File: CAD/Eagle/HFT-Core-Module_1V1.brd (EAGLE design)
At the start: 96.5 x 96.5 mm, 528 parts, among them Q0321 ABS07-32.768KHZ, Q1321 ABS07-32.768KHZ, Q2211 ABM3B-32.0000MHZ, Q2311 ABM3B-16.0000MHZ, T1051 MMBT2222, T1111 MMBT2222, T1121 MMBT2222, T1131 MMBT2222, U0111 STM32L4Z_144PIN_SMPS, U0521 PCAL6416APW, U0621 PCAL6416APW, U0711 IS25LP032D, U0721 IS25LP032D, U0801 CAT24C64, U0911 ZIO_EINK_1IN54, U1001 MIDAS_MCCOG21605B6W-FPTLWI, U1301 BNO085, U1401 BME680, U1501 LM4120IM5-3.0, U1511 MAX5217, U1531 CFPT-141-20MHZ, U1541 OPA354, U1542 LPV811, U1601 Si5338, U1651 TS5A23166, U1701 PCM1863, U1801 WM8523, U1901 SIM868, U2201 SX1262, U2271 PE4259, U2301 AX5243, U2401 LM53603-Q1, U2501 BQ24193, U2541 LPV811, U2601 BQ25570, U2681 TS5A23166, U2701 TPS62056, U2801 TPS62051, U2851 MCP4661-104E-MS, U2901 TS5A23166, U3001 TS5A23166, U3101 TS5A23166, U3201 TS5A23166, U3491 TS5A23166, U3492 TDK B4310, X1201 TTE_EN11-HSM, X1951 MICROSIM-8P_SDCARD-8P_MOLEX-1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, X2411 WIRE-TO-BOARD_5MM08_1X02, X2551 JST_S3B-XH-A, X2601 WIRE-TO-BOARD_5MM08_1X02, X3301 MOLEX 105017-0001, X3401 SMA_SMT_AMPHENOL-901-143, X3411 SAMTEC SMA-J-P-H-RA-TH1, X3471 SMA_SMT_AMPHENOL-901-143, SAM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, X3481 SMA_SMT_AMPHENOL-901-143, SAM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, X3491 SMA_SMT_AMPHENOL-901-143, SAM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, X3501 CUI SJ1-3535NS, X3511 CUI SJ1-3535NS, X3611 2X20/90_1MM27_HARWIN_M50-3202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, X3612 2X20/90_1MM27_HARWIN_M50-3202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, X3631 2X20/90_1MM27_HARWIN_M50-3202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, X3632 2X20/90_1MM27_HARWIN_M50-3202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

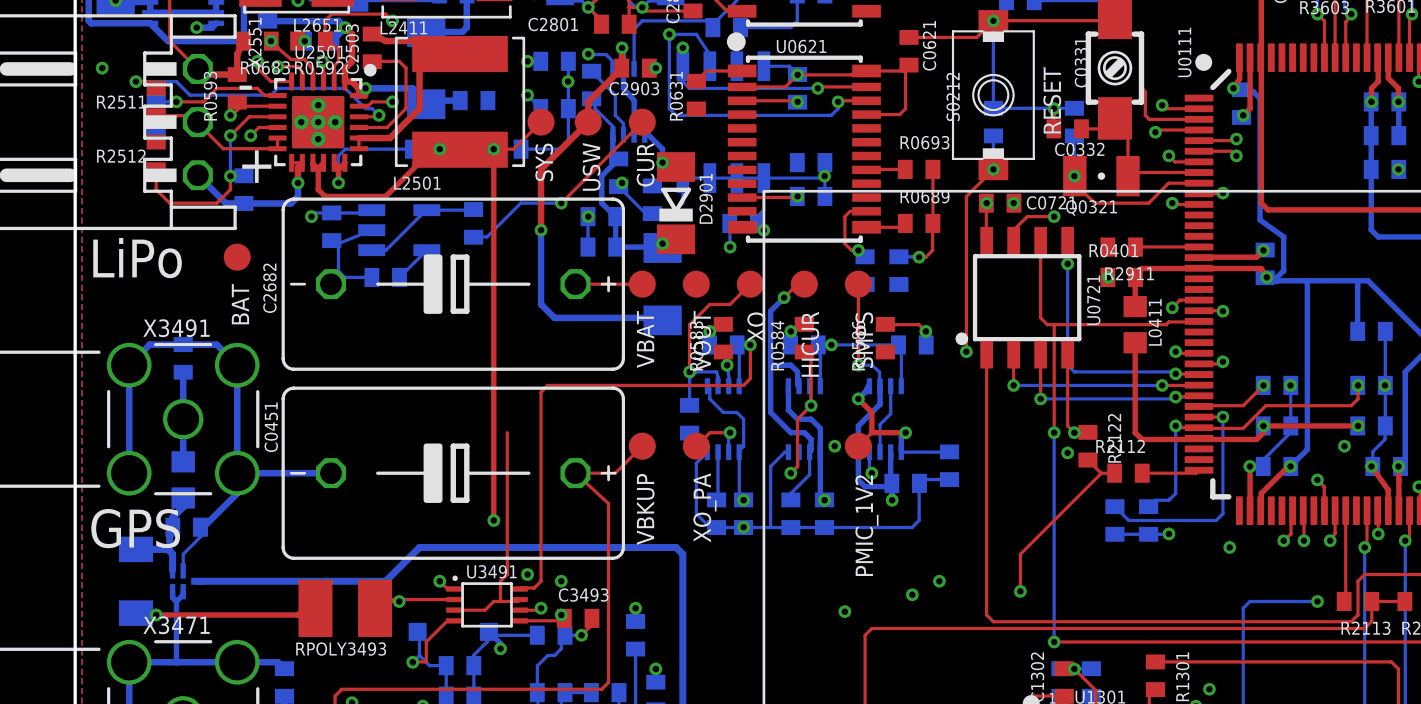
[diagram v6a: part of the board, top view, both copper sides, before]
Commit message: HW_1V1 - CAD/Eagle - MCU south complete
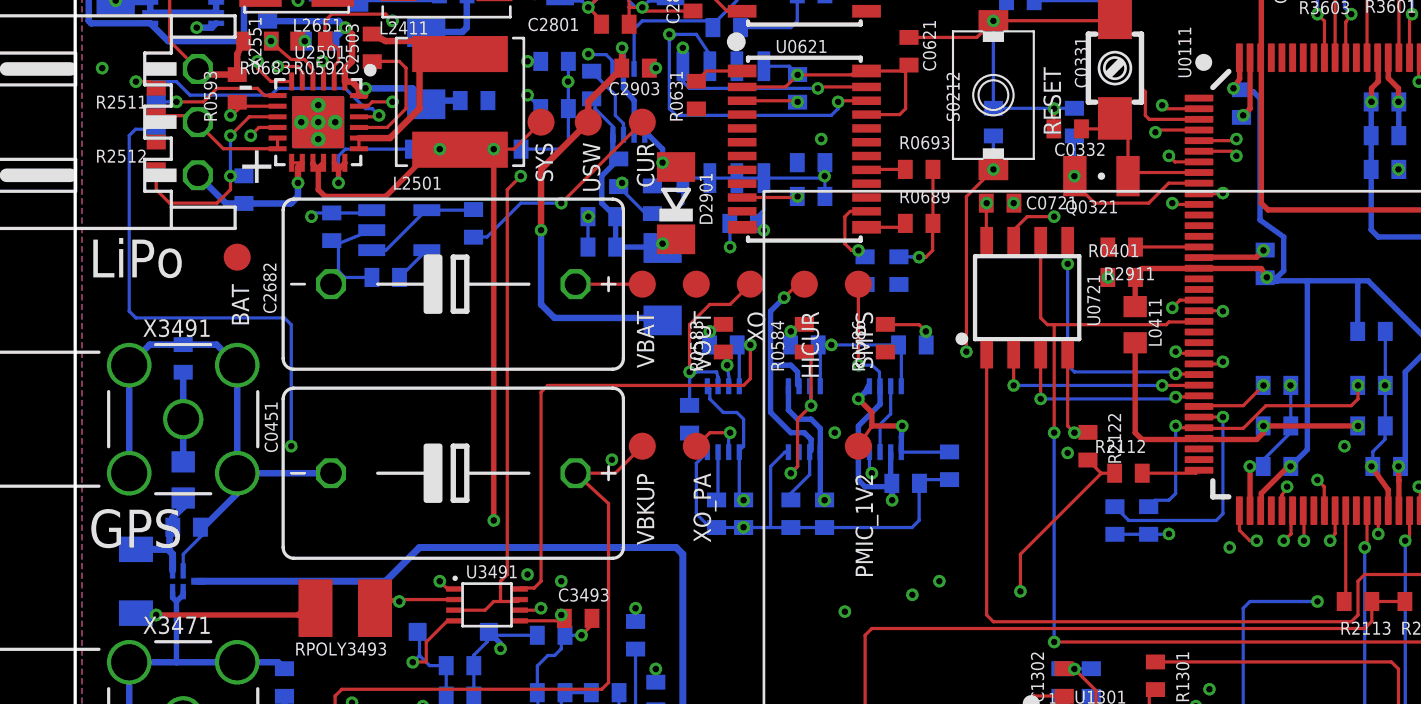
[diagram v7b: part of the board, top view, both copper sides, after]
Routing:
- net PA5: track 0.00 -> 72.1 mm, vias 0 -> 2
- net PA3: track 10.2 -> 57.6 mm, vias 1 -> 3
- net PEXPA_P1_2_R: track 13.7 -> 48.1 mm, vias 1 -> 3
- net PE3: track 76.8 -> 77.7 mm
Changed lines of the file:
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@@
 <wire x1="47.625" y1="53.0225" x2="46.6725" y2="53.0225" width="0.1524" layer="15"/>
 <via x="46.6725" y="53.0225" extent="1-16" drill="0.3"/>
-<wire x1="46.6725" y1="53.0225" x2="38.4175" y2="53.0225" width="0.1524" layer="3"/>
-<wire x1="38.4175" y1="53.0225" x2="38.1" y2="53.34" width="0.1524" layer="3"/>
-<wire x1="38.1" y1="53.34" x2="35.71875" y2="53.34" width="0.1524" layer="3"/>
-<via x="35.71875" y="53.34" extent="1-16" drill="0.3"/>
-<wire x1="35.71875" y1="53.34" x2="35.8775" y2="53.18125" width="0.1524" layer="15"/>
-<wire x1="35.8775" y1="53.18125" x2="35.8775" y2="50.4825" width="0.1524" layer="15"/>
+<wire x1="46.6725" y1="53.0225" x2="45.87875" y2="53.0225" width="0.1524" layer="3"/>
+<wire x1="45.87875" y1="53.0225" x2="45.24375" y2="53.6575" width="0.1524" layer="3"/>
+<wire x1="45.24375" y1="53.6575" x2="36.03625" y2="53.6575" width="0.1524" layer="3"/>
+<wire x1="36.03625" y1="53.6575" x2="35.71875" y2="53.975" width="0.1524" layer="3"/>
+<via x="35.71875" y="53.975" extent="1-16" drill="0.3"/>
+<wire x1="35.71875" y1="53.975" x2="35.8775" y2="53.81625" width="0.1524" layer="15"/>
+<wire x1="35.8775" y1="53.81625" x2="35.8775" y2="50.4825" width="0.1524" layer="15"/>
 <wire x1="35.56" y1="9.2225" x2="35.56" y2="13.6525" width="0.1524" layer="16"/>
 <wire x1="35.56" y1="13.6525" x2="36.03625" y2="14.12875" width="0.1524" layer="16"/>
@@
 <via x="22.86" y="64.77" extent="1-16" drill="0.3"/>
 <wire x1="22.86" y1="64.77" x2="26.67" y2="68.58" width="0.1524" layer="1"/>
-<wire x1="26.67" y1="68.58" x2="54.75" y2="50.31" width="0" layer="19" extent="1-1"/>
+<wire x1="54.75" y1="50.31" x2="54.75" y2="49.39" width="0.1524" layer="1"/>
+<wire x1="54.75" y1="49.39" x2="55.245" y2="48.895" width="0.1524" layer="1"/>
+<wire x1="55.245" y1="48.895" x2="55.5625" y2="48.895" width="0.1524" layer="1"/>
+<via x="55.5625" y="48.895" extent="1-16" drill="0.3"/>
+<wire x1="55.5625" y1="48.895" x2="55.245" y2="48.895" width="0.1524" layer="3"/>
+<wire x1="55.245" y1="48.895" x2="54.2925" y2="49.8475" width="0.1524" layer="3"/>
+<wire x1="54.2925" y1="49.8475" x2="41.275" y2="49.8475" width="0.1524" layer="3"/>
+<wire x1="41.275" y1="49.8475" x2="38.1" y2="53.0225" width="0.1524" layer="3"/>
+<wire x1="38.1" y1="53.0225" x2="32.385" y2="53.0225" width="0.1524" layer="3"/>
+<wire x1="32.385" y1="53.0225" x2="31.75" y2="52.3875" width="0.1524" layer="3"/>
+<wire x1="31.75" y1="52.3875" x2="25.55875" y2="52.3875" width="0.1524" layer="3"/>
+<wire x1="25.55875" y1="52.3875" x2="25.24125" y2="52.705" width="0.1524" layer="3"/>
+<via x="25.24125" y="52.705" extent="1-16" drill="0.3"/>
+<wire x1="25.24125" y1="52.705" x2="25.24125" y2="61.9125" width="0.1524" layer="15"/>
+<wire x1="25.24125" y1="61.9125" x2="22.86" y2="64.29375" width="0.1524" layer="15"/>
+<wire x1="22.86" y1="64.29375" x2="22.86" y2="64.77" width="0.1524" layer="15"/>
 </signal>
 <signal name="PA4">
@@
 <contactref element="U0111" pad="41"/>
 <contactref element="R2554" pad="1"/>
-<wire x1="3.81" y1="68.2475" x2="56.75" y2="50.31" width="0" layer="19" extent="1-16"/>
+<wire x1="56.75" y1="50.31" x2="56.75" y2="51.035" width="0.1524" layer="1"/>
+<wire x1="56.75" y1="51.035" x2="56.99125" y2="51.435" width="0.1524" layer="1"/>
+<via x="56.99125" y="51.435" extent="1-16" drill="0.3"/>
+<wire x1="56.99125" y1="51.435" x2="40.16375" y2="51.435" width="0.1524" layer="3"/>
+<wire x1="40.16375" y1="51.435" x2="38.25875" y2="53.34" width="0.1524" layer="3"/>
+<wire x1="38.25875" y1="53.34" x2="10.16" y2="53.34" width="0.1524" layer="3"/>
+<wire x1="3.81" y1="68.2475" x2="2.8425" y2="68.2475" width="0.1524" layer="16"/>
+<wire x1="2.8425" y1="68.2475" x2="2.54" y2="67.945" width="0.1524" layer="16"/>
+<wire x1="2.54" y1="67.945" x2="2.54" y2="59.69" width="0.1524" layer="16"/>
+<wire x1="2.54" y1="59.69" x2="2.8575" y2="59.3725" width="0.1524" layer="16"/>
+<wire x1="2.8575" y1="59.3725" x2="9.8425" y2="59.3725" width="0.1524" layer="16"/>
+<wire x1="9.8425" y1="59.3725" x2="10.16" y2="59.055" width="0.1524" layer="16"/>
+<wire x1="10.16" y1="59.055" x2="10.16" y2="53.34" width="0.1524" layer="16"/>
+<via x="10.16" y="53.34" extent="1-16" drill="0.3"/>
 </signal>
 <signal name="PA6">
@@
 <via x="64.77" y="51.435" extent="1-16" drill="0.3"/>
 <wire x1="64.77" y1="51.435" x2="66.04" y2="50.32375" width="0.1524" layer="15"/>
-<wire x1="66.04" y1="50.32375" x2="66.04" y2="47.9425" width="0.1524" layer="15"/>
-<wire x1="66.04" y1="47.9425" x2="64.135" y2="46.355" width="0.1524" layer="15"/>
+<wire x1="66.04" y1="50.32375" x2="66.04" y2="48.26" width="0.1524" layer="15"/>
+<wire x1="66.04" y1="48.26" x2="64.135" y2="46.355" width="0.1524" layer="15"/>
 <wire x1="64.135" y1="46.355" x2="64.135" y2="43.65625" width="0.1524" layer="15"/>
 <wire x1="64.135" y1="43.65625" x2="65.0875" y2="42.70375" width="0.1524" layer="15"/>
@@
 <wire x1="41.107" y1="53.06" x2="41.11625" y2="53.06925" width="0.1524" layer="16"/>
 <wire x1="38.85" y1="53.06" x2="38.85" y2="53.7725" width="0.254" layer="16"/>
-<wire x1="38.85" y1="53.7725" x2="39.0525" y2="53.975" width="0.254" layer="16"/>
-<via x="39.0525" y="53.975" extent="1-16" drill="0.3048"/>
-<wire x1="39.0525" y1="53.975" x2="37.465" y2="53.975" width="0.254" layer="1"/>
-<wire x1="37.465" y1="53.975" x2="36.83" y2="53.34" width="0.1524" layer="1"/>
-<wire x1="37.465" y1="53.975" x2="37.465" y2="54.9275" width="0.254" layer="1"/>
+<wire x1="38.85" y1="53.7725" x2="38.89375" y2="54.2925" width="0.254" layer="16"/>
+<via x="38.89375" y="54.2925" extent="1-16" drill="0.3048"/>
+<wire x1="38.89375" y1="54.2925" x2="37.465" y2="54.2925" width="0.254" layer="1"/>
+<wire x1="37.465" y1="54.2925" x2="36.83" y2="53.34" width="0.1524" layer="1"/>
+<wire x1="37.465" y1="54.2925" x2="37.465" y2="54.9275" width="0.254" layer="1"/>
 <wire x1="37.465" y1="54.9275" x2="36.83" y2="55.5625" width="0.254" layer="1"/>
 <via x="36.83" y="55.5625" extent="1-16" drill="0.3048"/>
@@
 <wire x1="20.0025" y1="46.0375" x2="20.0025" y2="46.99" width="0.1524" layer="1"/>
 <wire x1="20.0025" y1="46.99" x2="20.32" y2="47.3075" width="0.1524" layer="1"/>
-<wire x1="20.32" y1="47.3075" x2="20.32" y2="53.975" width="0.1524" layer="1"/>
 <wire x1="37.215" y1="75.195" x2="35.5075" y2="75.195" width="0.1524" layer="1"/>
 <wire x1="35.5075" y1="75.195" x2="35.2425" y2="74.6125" width="0.1524" layer="1"/>
 <via x="35.2425" y="74.6125" extent="1-16" drill="0.3"/>
+<wire x1="35.2425" y1="74.6125" x2="35.2425" y2="71.91375" width="0.1524" layer="15"/>
+<wire x1="35.2425" y1="71.91375" x2="35.56" y2="71.59625" width="0.1524" layer="15"/>
+<wire x1="35.56" y1="71.59625" x2="35.56" y2="70.00875" width="0.1524" layer="15"/>
+<wire x1="35.56" y1="70.00875" x2="35.08375" y2="69.5325" width="0.1524" layer="15"/>
+<wire x1="35.08375" y1="69.5325" x2="35.08375" y2="67.78625" width="0.1524" layer="15"/>
 <wire x1="35.2425" y1="74.6125" x2="35.2575" y2="74.6125" width="0" layer="19" extent="1-16"/>
-<wire x1="20.32" y1="53.975" x2="35.2425" y2="74.6125" width="0" layer="19" extent="1-1"/>
+<wire x1="20.32" y1="47.3075" x2="20.32" y2="65.405" width="0.1524" layer="1"/>
+<wire x1="20.32" y1="65.405" x2="20.955" y2="66.04" width="0.1524" layer="1"/>
+<via x="20.955" y="66.04" extent="1-16" drill="0.3"/>
+<wire x1="20.955" y1="66.04" x2="22.70125" y2="67.78625" width="0.1524" layer="3"/>
+<wire x1="22.70125" y1="67.78625" x2="35.08375" y2="67.78625" width="0.1524" layer="3"/>
+<via x="35.08375" y="67.78625" extent="1-16" drill="0.3"/>
 </signal>
 <signal name="PEXPA_P1_3_R">

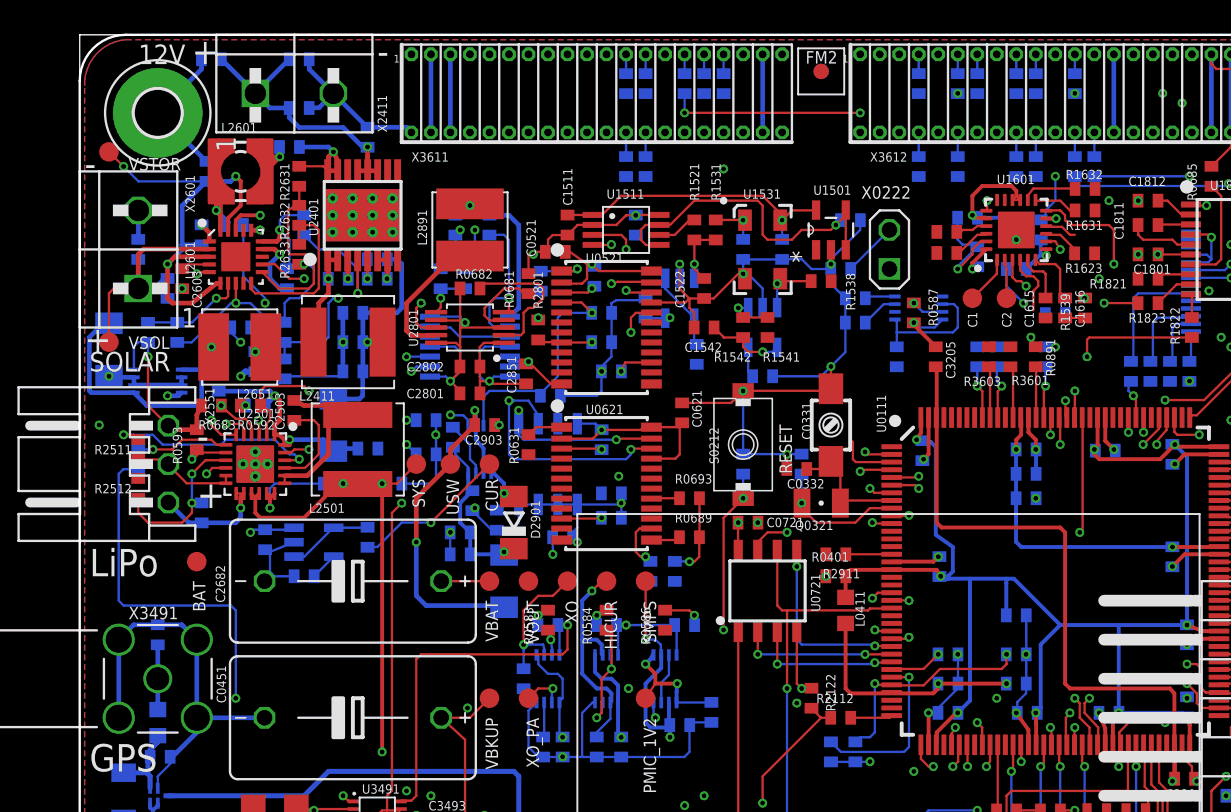
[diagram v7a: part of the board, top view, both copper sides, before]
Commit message: HW_1V1 - CAD/Eagle - MCU west complete
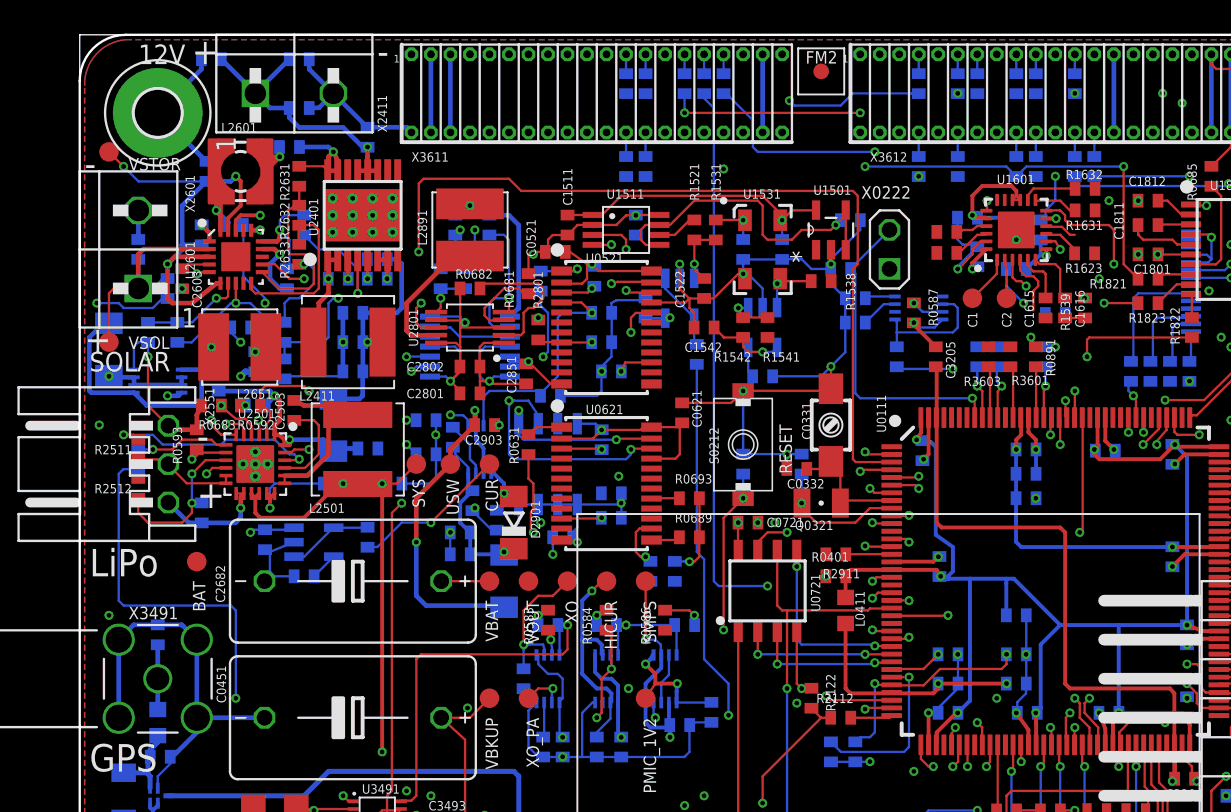
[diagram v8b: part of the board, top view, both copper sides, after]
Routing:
- net PA0: track 0.00 -> 78.9 mm, vias 0 -> 3
- net PE4: track 4.80 -> 69.4 mm, vias 1 -> 2
- net PF6: track 0.00 -> 43.9 mm, vias 0 -> 2
- net PE3: track 77.7 -> 121.3 mm, vias 4 -> 6
- net PF1: track 73.1 -> 116.4 mm, vias 2 -> 4
- net PF3: track 0.00 -> 41.5 mm, vias 0 -> 3
- net PC13: track 66.6 -> 101.2 mm, vias 2 -> 3
- net PA1: track 0.00 -> 34.5 mm, vias 0 -> 2
- net PF4: track 0.00 -> 29.1 mm, vias 0 -> 2
- net PH0: track 0.00 -> 23.6 mm, vias 0 -> 2
- net PF0: track 72.6 -> 95.6 mm, vias 2 -> 3
- net PH3_BOOT0: track 3.59 -> 20.9 mm, vias 0 -> 1
